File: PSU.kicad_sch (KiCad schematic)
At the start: 71 parts, among them U10 RT8293B, U14 TPS26400PWPR, U22 TLV77325PDBVR, U4 TPS7A39, U5 TPS560430XFDBVT

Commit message: last stm32h7 version
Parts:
- removed C106, C107, C108, C109, C110, C111, C53, C56: 100uF, PCM_JLCPCB:C_1206, symbol PCM_JLCPCB-Capacitors:1206,100uF
- removed C26, C33, C41, C42, C48, C49, C5, C7: 10uF, PCM_JLCPCB:C_0603, symbol PCM_JLCPCB-Capacitors:0603,10uF
- removed R119: 110k, Resistor_SMD:R_0402_1005Metric, symbol Device:R_Small
- removed R120: 8.2k, Resistor_SMD:R_0402_1005Metric, symbol Device:R_Small
- removed R130: 12k, Resistor_SMD:R_0402_1005Metric, symbol Device:R_Small
- removed R131: 20k, Resistor_SMD:R_0402_1005Metric, symbol Device:R_Small
- added C108, C109, C110, C111, C131, C156, C157, C158: 47uF, PCM_JLCPCB:C_1206, symbol PCM_JLCPCB-Capacitors:1206,47uF
- added C401: 1uF, PCM_JLCPCB:C_0402, symbol PCM_JLCPCB-Capacitors:0402,1uF
- added C402, C403, C404, C405: 10uF, PCM_JLCPCB:C_0603, symbol PCM_JLCPCB-Capacitors:0603,10uF,(2)
- added R401: 110kΩ, PCM_JLCPCB:R_0603, symbol PCM_JLCPCB-Resistors:0603,110kΩ
- added R402: 8.2kΩ, PCM_JLCPCB:R_0402, symbol PCM_JLCPCB-Resistors:0402,8.2kΩ
- added R403: 12kΩ, PCM_JLCPCB:R_0402, symbol PCM_JLCPCB-Resistors:0402,12kΩ
- added R404: 20kΩ, PCM_JLCPCB:R_0402, symbol PCM_JLCPCB-Resistors:0402,20kΩ
- added U301: STM32N657I0H3Q, User:VFBGA178_12X12_STM, symbol User:STM32N657I0H3Q
- L3: value 33u -> 22u
- U5: value TPS560430XFDBVT -> TI LMR54406DBVR
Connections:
- net +9V: now also R401.1
- net +V_OPA: now also C108.1, C109.1, C110.1, C111.1
- net -7V: now also C403.2, C405.2
- net -V_OPA: now also C131.2, C156.2, C157.2, C158.2
- net GND: now also C108.2, C109.2, C110.2, C111.2, C131.1, C156.1, C157.1, C158.1, C401.1, C402.2, C403.1, C404.2, C405.1, U301.A14 (VSS), U301.E2 (VSSAPMU), U301.E7 (VSS), U301.F1 (VSSSMPS), U301.F10 (VSS), U301.F2 (VSSSMPS), U301.F3 (VSSSMPS), U301.F4 (VSSSMPS), U301.F5 (VSSAON), U301.H10 (VSS), U301.H11 (VSS), U301.K10 (VSS), U301.K5 (VSS), U301.M4 (VSSA), U301.P1 (VSS), U301.P14 (VSS)
- net PowerPad: now also R403.2, R404.2
- net at U14.11 (ILIM): now also R404.1
- net +9VA: now reaches C129.1, D3.2, U14.15 (OUT), U14.16 (OUT)
- net +9VA: now also U4.1 (INP), U4.2 (EN), C402.1, C404.1
- net at U14.3 (UVLO): now also R401.2, R402.2
- net at U14.5 (OVP): now also R402.1, R403.1
- net at U4.3 (NR/SS): now also C401.2

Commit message: imrt1176 is added
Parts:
- removed C129: 10uF, PCM_JLCPCB:C_0603, symbol PCM_JLCPCB-Capacitors:0603,10uF,(2)
- removed C24: 4.7uF, PCM_JLCPCB:C_0805, symbol PCM_JLCPCB-Capacitors:0805,4.7uF
- removed C25, C4: 1uF, PCM_JLCPCB:C_0402, symbol PCM_JLCPCB-Capacitors:0402,1uF
- removed C27: 2.2nF, PCM_JLCPCB:C_0805, symbol PCM_JLCPCB-Capacitors:0805,2.2nF
- removed C28, C3, C6, C9: 100nF, PCM_JLCPCB:C_0402, symbol PCM_JLCPCB-Capacitors:0402,100nF,(2)
- removed C29: DNP, Capacitor_SMD:C_0805_2012Metric, symbol Device:C
- removed C30: C, Capacitor_SMD:C_0402_1005Metric, symbol Device:C
- removed C50, C65: C, symbol Device:C
- removed C57, C63, C80, C85: 10uF, PCM_JLCPCB:C_0402, symbol PCM_JLCPCB-Capacitors:0402,10uF
- removed D3: SMF20CA, PCM_JLCPCB:D_SOD-123FL, symbol PCM_JLCPCB-Diodes:TVS-Uni,SMF20CA
- removed FB3: ?, symbol Device:FerriteBead
- removed R3, R34: 47Ω, PCM_JLCPCB:R_0402, symbol PCM_JLCPCB-Resistors:0402,47Ω
- removed R31, R47: 24kΩ, PCM_JLCPCB:R_0402, symbol PCM_JLCPCB-Resistors:0402,24kΩ
- removed R32: 100kΩ, PCM_JLCPCB:R_0402, symbol PCM_JLCPCB-Resistors:0402,100kΩ
- removed R33: 22kΩ, PCM_JLCPCB:R_0402, symbol PCM_JLCPCB-Resistors:0402,22kΩ
- removed R401: 110kΩ, PCM_JLCPCB:R_0603, symbol PCM_JLCPCB-Resistors:0603,110kΩ
- removed R402: 8.2kΩ, PCM_JLCPCB:R_0402, symbol PCM_JLCPCB-Resistors:0402,8.2kΩ
- removed R403: 12kΩ, PCM_JLCPCB:R_0402, symbol PCM_JLCPCB-Resistors:0402,12kΩ
- removed R404: 20kΩ, PCM_JLCPCB:R_0402, symbol PCM_JLCPCB-Resistors:0402,20kΩ
- removed R46: 75kΩ, PCM_JLCPCB:R_0402, symbol PCM_JLCPCB-Resistors:0402,75kΩ
- removed R6: 4.3kΩ, PCM_JLCPCB:R_0603, symbol PCM_JLCPCB-Resistors:0603,4.3kΩ
- removed U10: RT8293B, Package_SO:TI_SO-PowerPAD-8, symbol User:RT8293B
- removed U14: TPS26400PWPR, User:PWP0016H-IPC_A, symbol 2025-02-23_17-32-12:TPS26400PWPR
- removed U301: STM32N657I0H3Q, User:VFBGA178_12X12_STM, symbol User:STM32N657I0H3Q
- removed U5: TI LMR54406DBVR, Package_TO_SOT_SMD:SOT-23-6, symbol User:TPS560430XF
- added C1, C19, C2, C20, C21, C22, C23, C24, C36, C37, C38, C39, C44, C48, C49, C5, C6, C7, C9: 10uF, PCM_JLCPCB:C_0402, symbol PCM_JLCPCB-Capacitors:0402,10uF
- added C11: 220nF, PCM_JLCPCB:C_0402, symbol PCM_JLCPCB-Capacitors:0402,220nF
- added C17, C18: 2.2nF, PCM_JLCPCB:C_0805, symbol PCM_JLCPCB-Capacitors:0805,2.2nF
- added C25, C26: 10u, Capacitor_SMD:C_1206_3216Metric, symbol Device:C_Small
- added C27: 100n, Capacitor_SMD:C_0603_1608Metric, symbol Device:C_Small
- added C28: 10n, Capacitor_SMD:C_0603_1608Metric, symbol Device:C_Small
- added C29: 6p8, Capacitor_SMD:C_0603_1608Metric, symbol Device:C_Small
- added C3, C4, C8: 100nF, PCM_JLCPCB:C_0402, symbol PCM_JLCPCB-Capacitors:0402,100nF
- added C30: 8p2, Capacitor_SMD:C_0603_1608Metric, symbol Device:C_Small
- added C31: 220n, Capacitor_SMD:C_0603_1608Metric, symbol Device:C_Small
- added C32, C33: 22u, Capacitor_SMD:C_0805_2012Metric, symbol Device:C_Small
- added C34: 4n7, Capacitor_SMD:C_0603_1608Metric, symbol Device:C_Small
- added C40, C42, C43, C45, C47: 2.2uF, PCM_JLCPCB:C_0402, symbol PCM_JLCPCB-Capacitors:0402,2.2uF
- added C41: 4.7uF, PCM_JLCPCB:C_0402, symbol PCM_JLCPCB-Capacitors:0402,4.7uF
- added C53, C56: 100nF, PCM_JLCPCB:C_0603, symbol PCM_JLCPCB-Capacitors:0603,100nF
- added D4, D5: B5819W, Diode_SMD:D_SOD-123, symbol Device:D_Schottky_Small
- added IC1: TPS65131RGET, symbol User:TPS65131RGET
- added J3: 9V, User:BarrelJack_GCT_DCJ200-10-A_Horizontal, symbol Connector:Jack-DC
- added L1: 4.7uH, symbol Device:L
- added L6, L7: 10u, Inductor_SMD:L_Sunlord_MWSA0518_5.4x5.2mm, symbol Device:L_Small
- added Q1: NMOS, symbol Simulation_SPICE:NMOS
- added Q2: AO3401A, Package_TO_SOT_SMD:SOT-23, symbol Transistor_FET:AO3401A
- added R11: 22kΩ, PCM_JLCPCB:R_0805, symbol PCM_JLCPCB-Resistors:0805,22kΩ
- added R17: 33kΩ, PCM_JLCPCB:R_0402, symbol PCM_JLCPCB-Resistors:0402,33kΩ
- added R18: 100kΩ, PCM_JLCPCB:R_0402, symbol PCM_JLCPCB-Resistors:0402,100kΩ
- added R2: 47Ω, PCM_JLCPCB:R_0402, symbol PCM_JLCPCB-Resistors:0402,47Ω
- added R23: 100, Resistor_SMD:R_0603_1608Metric, symbol Device:R_Small
- added R24, R27: 1M, Resistor_SMD:R_0603_1608Metric, symbol Device:R_Small
- added R25: 110k, Resistor_SMD:R_0603_1608Metric, symbol Device:R_Small
- added R26: 100k, Resistor_SMD:R_0603_1608Metric, symbol Device:R_Small
- added R28, R29: 12k, Resistor_SMD:R_0603_1608Metric, symbol Device:R_Small
- added R5: 75kΩ, PCM_JLCPCB:R_0402, symbol PCM_JLCPCB-Resistors:0402,75kΩ
- added R7: 4.7kΩ, PCM_JLCPCB:R_0402, symbol PCM_JLCPCB-Resistors:0402,4.7kΩ
- added R8: 24kΩ, PCM_JLCPCB:R_0402, symbol PCM_JLCPCB-Resistors:0402,24kΩ
- added TP1: 3.3V_Prefilter, symbol Connector:TestPoint
- added TP2: Bode, symbol Connector:TestPoint
- added TP3: FB, symbol Connector:TestPoint
- added TP4: 3.3V_GND, symbol Connector:TestPoint
- added TP5: 3.3V_Postfilter, symbol Connector:TestPoint
- added U11: RT8293B, Package_SO:SOP-8-1EP_4.57x4.57mm_P1.27mm_EP4.57x4.45mm_ThermalVias, symbol User:RT8293B
- added U13: LM74700, Package_TO_SOT_SMD:SOT-23-6, symbol Power_Management:LM74700
- added U6: MIMXRT1176CVM8A, User:BGA289C80P17X17_1400X1400X152, symbol User:MIMXRT1176CVM8A
- L3: value 22u -> 4.7uf; footprint (none) -> Inductor_SMD:L_12x12mm_H8mm
- L4: value 3.6uH -> L; footprint Inductor_SMD:L_Cenker_CKCS8040 -> (none)
- renumbered C68 to C10, C69 to C62, U22 to U8
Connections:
- net +9V is gone; now on net +9VA: D1.1
- net +3.3V: now also C51.1, L2.2, R56.1, C1.1, C2.1, C44.1, C5.1, C7.1, R17.1, TP5.1, U6.L5 (DCDC_IN_Q), U6.M5 (DCDC_IN), U6.N5 (DCDC_IN), U6.R12 (VDD_LPSR_IN), U6.U12 (VDD_SNVS_IN); no longer C35.1, L4.2
- net +9VA: now also C53.1, C56.1, J3.2, Q1.3 (S), U13.3 (EN), U13.6 (ANODE)
- net at L4.1: now also C54.1, Q1.1 (D), U13.4 (CATHODE)
- net at L3.1: now also C3.2, U11.3 (SW)
- net at L2.1: now also L3.2, C19.1, C20.1, C21.1, C22.1, R2.2, TP1.1; no longer C54.1
- net +2.5VA renamed +2.5V
- net +9-18V: no longer names the net of R12.1
- net +9-18V: now also L4.2, C23.1, C48.1, C49.1, R18.1, U11.2 (VIN); no longer L2.2
- net +V_OPA renamed +6.5V
- net -V_OPA renamed -6.5V
- net GND renamed DCDC_GND
- net DCDC_GND: now also C1.2, C11.2, C18.2, C19.2, C2.2, C20.2, C21.2, C22.2, C23.2, C24.2, C25.2, C26.2, C27.2, C28.2, C31.2, C32.2, C33.2, C34.2, C36.2, C37.2, C38.2, C39.2, C4.2, C40.2, C41.2, C42.2, C43.2, C44.2, C45.2, C47.2, C48.2, C49.2, C5.2, C53.2, C6.2, C7.2, C8.2, C9.2, IC1.19 (AGND), IC1.2 (PGND_1), IC1.25 (POWERPAD), IC1.3 (PGND_2), J3.1, L7.2, R11.2, R25.1, R28.1, R29.1, R7.2, R8.2, TP4.1, U11.4 (GND), U11.9 (GND), U6.A1 (VSS1), U6.A17 (VSS1), U6.B7 (VSS1), U6.C10 (VSS1), U6.C12 (VSS1), U6.C14 (VSS1), U6.C8 (VSS1), U6.D4 (VSS1), U6.F11 (VSS1), U6.F12 (VSS1), U6.F13 (VSS1), U6.G10 (VSS2), U6.G11 (VSS2), U6.G15 (VSS2), U6.G3 (VSS1), U6.G7 (VSS1), U6.G8 (VSS1), U6.G9 (VSS1), U6.H11 (VSS2), U6.H7 (VSS2), U6.J11 (VSS2), U6.J7 (VSS2), U6.K11 (VSS2), U6.K6 (DCDC_GND), U6.K7 (DCDC_GND), U6.L10 (VSS2), U6.L11 (VSS2), U6.L15 (VSS2), U6.L3 (VSS2), U6.L6 (DCDC_GND), U6.P14 (VSS2), U6.P4 (VSS2), U6.R4 (VSS2), U6.R7 (VSS3), U6.T11 (TEST_MODE), U6.T12 (VSS3), U6.U1 (VSS3), U6.U17 (VSS3); no longer L3.2
- new net: IC1.7 (BSW), Q2.1 (G)
- new net: C26.1, L6.1, Q2.3 (D)
- new net: C29.2, IC1.22 (FBP), R24.1, R25.2
- new net: C27.1, IC1.10 (ENN), IC1.11 (PSN), IC1.4 (VIN), IC1.8 (ENP), IC1.9 (PSP), R23.1
- new net: C17.2, R11.1
- new net: C3.1, U11.1 (BOOT)
- new net: R5.2, R8.1, TP3.1, U11.5 (FB)
- new net: C17.1, C18.1, U11.6 (COMP)
- new net: R18.2, U11.7 (EN)
- new net: C4.1, U11.8 (SS/PG)
- new net: L1.1, U6.T3 (DCDC_LP), U6.U3 (DCDC_LP)
- new net: L1.2, U6.T4 (DCDC_LN), U6.U4 (DCDC_LN)
- new net: D5.1 (K), IC1.13 (OUTN_1), IC1.14 (OUTN_2), L7.1
- new net: C11.1, R17.2, U6.P3 (DCDC_PSWITCH)
- new net: C30.1, IC1.16 (FBN), R26.1, R27.2
- new net: D4.2 (A), IC1.1 (INP_1), IC1.24 (INP_2), L6.2
- new net: C31.1, IC1.17 (VREF), R26.2
- new net: C34.1, IC1.18 (CN)
- new net: C28.1, IC1.21 (CP)
- new net: U6.F6 (NVCC_EMC1), U6.F7 (NVCC_EMC1), U6.G6 (NVCC_EMC1)
- new net: U6.H6 (NVCC_EMC2), U6.J6 (NVCC_EMC2)
- new net: C56.2, U13.1 (VCAP)
- new net: Q1.2 (G), U13.5 (GATE)
- new net: R2.1, R5.1, TP2.1
- new net +12V: C29.1, C33.1, D4.1 (K), IC1.23 (VPOS), R24.2, R29.2
- new net +5V: C25.1, IC1.5 (INN_1), IC1.6 (INN_2), Q2.2 (S), R23.2
- new net -12V: C30.2, C32.1, D5.2 (A), IC1.15 (VNEG), R27.1, R28.2
- new net 1.15V_DCDC: C24.1, C35.1, C36.1, C37.1, C38.1, C39.1, U6.K8 (DCDC_DIG), U6.K9 (DCDC_DIG), U6.L7 (DCDC_DIG_SENSE), U6.L8 (DCDC_DIG)
- new net 1.8V_DCDC: C6.1, C9.1, U6.F9 (VDD_MIPI_1P8), U6.M6 (DCDC_ANA_SENSE), U6.M7 (DCDC_ANA), U6.M8 (DCDC_ANA)
- new net DCDC_MODE: C8.1, R7.1, U6.N4 (DCDC_MODE)
- new net VDDA_1P0: C42.1, C43.1, U6.F10 (VDD_MIPI_1P0), U6.N11 (VDDA_1P0)
- new net VDD_LPSR_ANA: C40.1, U6.P12 (VDD_LPSR_ANA)
- new net VDD_LPSR_DIG: C41.1, U6.P11 (VDD_LPSR_DIG)
- new net VDD_SNVS_ANA: C45.1, C47.1, U6.U11 (NVCC_SNVS), U6.U14 (VDD_SNVS_ANA)
- new net VDD_SOC_IN: U6.H10 (VDD_SOC_IN), U6.H8 (VDD_SOC_IN), U6.H9 (VDD_SOC_IN), U6.J10 (VDD_SOC_IN), U6.J8 (VDD_SOC_IN), U6.J9 (VDD_SOC_IN), U6.K10 (VDD_SOC_IN)
- no-connect marks 6 -> 2
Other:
- note added: "+V_OPA 6.5V 50mA -V_OPA -6.5V 50mA +3.3V 3.3V 500mA +1.8V 1.8V 1.2A"
- note added: "5V to +12V / -12V Regulator"
- note added: "9V 50+200+330+100"
- note added: "VCC(max) = 12V - Limited by Vgs (Q1)!"
- note added: "https://www.we-online.com/components/products/datasheet/7447713047.pdf"
- note removed: "-kisebb MOSFET U21-re -TP2121 ellenállásait kiszámolni -dc-dc be- és kimenő szűrő kiszámolni -tps7a39 ellenállásait kiszámolni +-5V-os konverternek kimenő szűrőt tervezni"
- note removed: "OMRON G6K-2F-Y-TR DC5"
- note removed: "https://www.ti.com/lit/an/slvae10/slvae10.pdf?utm_source=chatgpt.com&ts=1755168580112&ref_url=https%253A%252F%252Fchatgpt.com%252F"
- moved on the sheet: C10, C51, C52, C54, C55, C62, D1, L2, R12, R56, U8

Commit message: added renesas RA8P1
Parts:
- removed C1, C2, C23, C24, C35, C36, C37, C38, C39, C44, C48, C49, C5, C6, C7, C9: 10uF, PCM_JLCPCB:C_0402, symbol PCM_JLCPCB-Capacitors:0402,10uF
- removed C11: 220nF, PCM_JLCPCB:C_0402, symbol PCM_JLCPCB-Capacitors:0402,220nF
- removed C40, C42, C43, C45, C47: 2.2uF, PCM_JLCPCB:C_0402, symbol PCM_JLCPCB-Capacitors:0402,2.2uF
- removed C53, C56: 100nF, PCM_JLCPCB:C_0603, symbol PCM_JLCPCB-Capacitors:0603,100nF
- removed C8: 100nF, PCM_JLCPCB:C_0402, symbol PCM_JLCPCB-Capacitors:0402,100nF
- removed Q1: NMOS, symbol Simulation_SPICE:NMOS
- removed R17: 33kΩ, PCM_JLCPCB:R_0402, symbol PCM_JLCPCB-Resistors:0402,33kΩ
- removed R7: 4.7kΩ, PCM_JLCPCB:R_0402, symbol PCM_JLCPCB-Resistors:0402,4.7kΩ
- removed U13: LM74700, Package_TO_SOT_SMD:SOT-23-6, symbol Power_Management:LM74700
- removed U6: MIMXRT1176CVM8A, User:BGA289C80P17X17_1400X1400X152, symbol User:MIMXRT1176CVM8A
- added C1, C11, C2, C24, C35, C36, C37, C38, C39, C40, C42, C43, C44, C45, C47, C5, C6, C60, C64, C65, C68, C69, C7, C70, C71, C72, C73, C74, C75, C8, C9: 4.7uF, PCM_JLCPCB:C_0402, symbol PCM_JLCPCB-Capacitors:0402,4.7uF
- added C23, C48, C49, C81: 10uF, PCM_JLCPCB:C_0805, symbol PCM_JLCPCB-Capacitors:0805,10uF,(2)
- added D6: SS14, PCM_JLCPCB:D_SMA, symbol PCM_JLCPCB-Diodes:Schottky,SS14
- added F1: 1A, Fuse:Fuse_0805_2012Metric, symbol Device:Fuse
- added IC2: R7KA8P1KFLCAB#UC0, User:BGA-225_15x15_11.0x11.0mm, symbol User:R7KA8P1KFLCAB#UC0
- C41: Stock 4921316 -> 4366811
- L1: footprint (none) -> Inductor_SMD:L_Wuerth_MAPI-4030
- L4: value L -> 1uH; footprint (none) -> Inductor_SMD:L_1008_2520Metric
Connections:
- net VDD_LPSR_DIG is gone; now on net +3.3V: C41.1
- net +3.3V: now also C1.1, C11.1, C2.1, C24.1, C35.1, C36.1, C37.1, C38.1, C39.1, C40.1, C42.1, C43.1, C44.1, C45.1, C5.1, C6.1, C7.1, C70.1, C8.1, C9.1, IC2.A10 (VCC_DCDC_2), IC2.A9 (VCC_DCDC_1), IC2.B10 (VCC_DCDC_4), IC2.B9 (VCC_DCDC_3), IC2.E10 (VCC_07), IC2.E5 (VCC_08), IC2.F14 (VCC_05), IC2.F5 (VCC_09), IC2.G12 (VCC_03), IC2.G13 (VCC_USBHS), IC2.G5 (VCC_10), IC2.J12 (VCC_02), IC2.J13 (AVCC_USBHS), IC2.J6 (VCC2_15), IC2.K13 (VCC_01), IC2.K5 (VCC2_14), IC2.L14 (VBATT), IC2.N1 (VCC2_12), IC2.R15 (VCC_USB)
- net at L4.2, R12.1, R18.1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: now also C23.1, C48.1, C49.1, C81.1
- net at L1.1: now also C47.1, C60.1, C64.1, C65.1, C68.1, C69.1, C71.1, C72.1, C73.1, C74.1, C75.1, IC2.E8 (VCL5), IC2.F8 (VCL6), IC2.F9 (VCL4), IC2.G8 (VCL7), IC2.G9 (VCL3), IC2.H8 (VCL8), IC2.H9 (VCL2), IC2.J8 (VCL9), IC2.J9 (VCL1), IC2.K8 (VCL10), IC2.K9 (VCL0), IC2.L9 (VCL11)
- net at L1.2: now also IC2.A6 (VLO_1), IC2.A7 (VLO_2), IC2.B6 (VLO_3), IC2.B7 (VLO_4)
- net +9VA renamed +7V
- net +7V: no longer D1.1, J3.2
- net DCDC_GND renamed GND
- net GND: now also C1.2, C11.2, C2.2, C23.2, C24.2, C35.2, C36.2, C37.2, C38.2, C39.2, C40.2, C42.2, C43.2, C44.2, C45.2, C47.2, C48.2, C49.2, C5.2, C6.2, C60.2, C64.2, C65.2, C68.2, C69.2, C7.2, C70.2, C71.2, C72.2, C73.2, C74.2, C75.2, C8.2, C81.2, C9.2, IC2.A8 (VSS_DCDC_1), IC2.B8 (VSS_DCDC_2), IC2.E6 (VSS_08), IC2.E7 (VSS5), IC2.E9 (VSS_07), IC2.F10 (VSS4), IC2.F13 (VSS_03), IC2.F15 (VSS_05), IC2.F6 (VSS_09), IC2.F7 (VSS6), IC2.G10 (VSS3), IC2.G6 (VSS_10), IC2.G7 (VSS7), IC2.H10 (VSS2), IC2.H12 (VSS_02), IC2.H14 (VSS2_USBHS), IC2.H15 (VSS1_USBHS), IC2.H6 (VSS_15), IC2.H7 (VSS8), IC2.J10 (VSS1), IC2.J7 (VSS9), IC2.K10 (VSS0), IC2.K6 (VSS_14), IC2.K7 (VSS10), IC2.L15 (VSS_01), IC2.L8 (VSS11), IC2.N3 (VSS_MIPI), IC2.N9 (AVSS0), IC2.P15 (VSS_USB), IC2.P8 (VREFL), IC2.P9 (VREFL0), IC2.R4 (VSS_12)
- new net: D1.1, D6.2, J3.2
- new net: D6.1, F1.1
- no-connect marks 2 -> 3
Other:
- note added: "TPS2596"
- moved on the sheet: C10, C62, D1, L1, U8

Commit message: progressed with SDRAM layout
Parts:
- removed C10: 10uF, PCM_JLCPCB:C_0402, symbol PCM_JLCPCB-Capacitors:0402,10uF
- removed C25, C26: 10u, Capacitor_SMD:C_1206_3216Metric, symbol Device:C_Small
- removed C27: 100n, Capacitor_SMD:C_0603_1608Metric, symbol Device:C_Small
- removed C28: 10n, Capacitor_SMD:C_0603_1608Metric, symbol Device:C_Small
- removed C29: 6p8, Capacitor_SMD:C_0603_1608Metric, symbol Device:C_Small
- removed C3: 100nF, PCM_JLCPCB:C_0402, symbol PCM_JLCPCB-Capacitors:0402,100nF
- removed C30: 8p2, Capacitor_SMD:C_0603_1608Metric, symbol Device:C_Small
- removed C31: 220n, Capacitor_SMD:C_0603_1608Metric, symbol Device:C_Small
- removed C32, C33: 22u, Capacitor_SMD:C_0805_2012Metric, symbol Device:C_Small
- removed C34: 4n7, Capacitor_SMD:C_0603_1608Metric, symbol Device:C_Small
- removed C402, C403: 10uF, PCM_JLCPCB:C_0603, symbol PCM_JLCPCB-Capacitors:0603,10uF,(2)
- removed C51, C54: C, symbol Device:C
- removed C55: ?, symbol Device:C_Polarized
- removed D4, D5: B5819W, Diode_SMD:D_SOD-123, symbol Device:D_Schottky_Small
- removed F1: 1A, Fuse:Fuse_0805_2012Metric, symbol Device:Fuse
- removed L2: L, symbol Device:L
- removed Q2: AO3401A, Package_TO_SOT_SMD:SOT-23, symbol Transistor_FET:AO3401A
- removed R12: 0Ω, PCM_JLCPCB:R_0402, symbol PCM_JLCPCB-Resistors:0402,0Ω
- removed R23: 100, Resistor_SMD:R_0603_1608Metric, symbol Device:R_Small
- removed R24, R27: 1M, Resistor_SMD:R_0603_1608Metric, symbol Device:R_Small
- removed R25: 110k, Resistor_SMD:R_0603_1608Metric, symbol Device:R_Small
- removed R26: 100k, Resistor_SMD:R_0603_1608Metric, symbol Device:R_Small
- removed R28, R29: 12k, Resistor_SMD:R_0603_1608Metric, symbol Device:R_Small
- removed R56: 0, symbol Device:R_Small
- added C10, C30: 4.7uF, PCM_JLCPCB:C_0402, symbol PCM_JLCPCB-Capacitors:0402,4.7uF
- added C106, C107: 6.8pF, PCM_JLCPCB:C_0402, symbol PCM_JLCPCB-Capacitors:0402,6.8pF
- added C25, C26, C28, C29: 10uF, PCM_JLCPCB:C_0402, symbol PCM_JLCPCB-Capacitors:0402,10uF
- added C27, C3, C54, C84, C85, C86: 100nF, PCM_JLCPCB:C_0402, symbol PCM_JLCPCB-Capacitors:0402,100nF,(2)
- added C31: 220nF, PCM_JLCPCB:C_0402, symbol PCM_JLCPCB-Capacitors:0402,220nF
- added C32, C33, C34, C51, C55, C94, C95, C96: 47uF, PCM_JLCPCB:C_1206, symbol PCM_JLCPCB-Capacitors:1206,47uF
- added C53: 1uF, PCM_JLCPCB:C_0603, symbol PCM_JLCPCB-Capacitors:0603,1uF
- added C82, C83: 10uF, PCM_JLCPCB:C_0805, symbol PCM_JLCPCB-Capacitors:0805,10uF,(2)
- added C97: 10nF, Capacitor_SMD:C_0603_1608Metric, symbol Device:C
- added C98: 4.7nF, Capacitor_SMD:C_0603_1608Metric, symbol Device:C
- added D4, D7: B5819W, PCM_JLCPCB:D_SOD-123, symbol PCM_JLCPCB-Diodes:Schottky,B5819W
- added Q1: AO3401A, PCM_JLCPCB:Q_SOT-23, symbol PCM_JLCPCB-Transistors:PMOS,AO3401A
- added R12: 1, PCM_JLCPCB:R_0402, symbol Device:R
- added R23, R25: 47Ω, PCM_JLCPCB:R_0402, symbol PCM_JLCPCB-Resistors:0402,47Ω
- added R24: 100Ω, PCM_JLCPCB:R_0603, symbol PCM_JLCPCB-Resistors:0603,100Ω
- added R26, R28: 100kΩ, PCM_JLCPCB:R_0402, symbol PCM_JLCPCB-Resistors:0402,100kΩ
- added R27, R48: 510kΩ, PCM_JLCPCB:R_0402, symbol PCM_JLCPCB-Resistors:0402,510kΩ
- added R44: 12kΩ, PCM_JLCPCB:R_0402, symbol PCM_JLCPCB-Resistors:0402,12kΩ
- added R45: 110kΩ, PCM_JLCPCB:R_0603, symbol PCM_JLCPCB-Resistors:0603,110kΩ
- added R46: 8.2kΩ, PCM_JLCPCB:R_0603, symbol PCM_JLCPCB-Resistors:0603,8.2kΩ
- added R47: 1.5kΩ, PCM_JLCPCB:R_0402, symbol PCM_JLCPCB-Resistors:0402,1.5kΩ
- added TP10: FB3, Thunderscope_Rev5.1:GEN_TP_PCB, symbol Connector:TestPoint
- added TP6: Bode3, Thunderscope_Rev5.1:GEN_TP_PCB, symbol Connector:TestPoint
- added TP7: 7V, Thunderscope_Rev5.1:GEN_TP_PCB, symbol Connector:TestPoint
- added TP8: -7V, Thunderscope_Rev5.1:GEN_TP_PCB, symbol Connector:TestPoint
- added TP9: FB2, Thunderscope_Rev5.1:GEN_TP_PCB, symbol Connector:TestPoint
- added U13: TPS259630, Package_SO:TI_SO-PowerPAD-8, symbol User:TPS259630
- C52: value ? -> 100u, 60mR; footprint (none) -> Capacitor_Tantalum_SMD:CP_EIA-7343-31_Kemet-D
- L3: footprint Inductor_SMD:L_12x12mm_H8mm -> User:WE-PD_1030P
- L4: value 1uH -> 22uH; footprint Inductor_SMD:L_1008_2520Metric -> Inductor_SMD:L_7.3x7.3_H3.5
- L6, L7: footprint Inductor_SMD:L_Sunlord_MWSA0518_5.4x5.2mm -> Inductor_SMD:L_Sunlord_MWSA0518S
- TP1: value 3.3V_Prefilter -> 3.3V; footprint (none) -> Thunderscope_Rev5.1:GEN_TP_PCB
- TP2, TP3: footprint (none) -> Thunderscope_Rev5.1:GEN_TP_PCB
- TP4: footprint (none) -> TestPoint:TestPoint_Pad_1.0x1.0mm
- TP5: value 3.3V_Postfilter -> Bode2; footprint (none) -> Thunderscope_Rev5.1:GEN_TP_PCB
- U17: renamed from IC1; footprint (none) -> Package_DFN_QFN:VQFN-24-1EP_4x4mm_P0.5mm_EP2.5x2.5mm_ThermalVias
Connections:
- net +12V is gone; now on net +7V: U17.23 (VPOS)
- net +5V is gone; now on net +3.3V: U17.5 (IN_N), U17.6 (IN_N_2)
- net -12V is gone; now on net -7V: U17.15 (VNEG)
- net +2.5V: now also IC2.N8 (AVCC0), IC2.R8 (VREFH), IC2.R9 (VREFH0)
- net +3.3V: now also C19.1, C20.1, C21.1, C22.1, IC2.P4 (AVCC_MIPI), L3.2, R2.2, TP1.1, C10.1, C30.1, Q1.2 (S); no longer TP5.1
- net +7V: now also C55.1, C94.1, C95.1, C96.1, D7.1, R23.2, TP7.1
- net -7V: now also C32.2, C33.2, C34.2, C51.2, D4.2, R25.1, TP8.1
- net GND: now also U17.11 (PSN), U17.9 (PSP), C10.2, C25.2, C26.2, C27.2, C28.2, C29.2, C30.2, C31.1, C32.1, C33.1, C34.1, C51.1, C53.2, C54.2, C55.2, C82.2, C83.2, C84.2, C85.2, C86.2, C94.2, C95.2, C96.2, C97.2, C98.2, R26.2, R46.2, R47.2, U13.1 (GND), U13.9 (EPAD)
- net at U17.7 (BSW): now also Q1.1 (G)
- net at L6.1: now also C26.1, C28.1, C29.1, Q1.3 (D)
- net at U17.22 (FBP): now also C106.2, R26.1, R48.1, TP9.1
- net MCU_DCDC_OUT: now reaches C47.1, C60.1, C64.1, C65.1, C68.1, C69.1, C71.1, C72.1, C73.1, C74.1, C75.1, IC2.E8 (VCL5), IC2.F8 (VCL6), IC2.F9 (VCL4), IC2.G8 (VCL7), IC2.G9 (VCL3), IC2.H8 (VCL8), IC2.H9 (VCL2), IC2.J8 (VCL9), IC2.J9 (VCL1), IC2.K8 (VCL10), IC2.K9 (VCL0), IC2.L9 (VCL11), L1.1
- net at C23.1, C48.1, C49.1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: now also C82.1, C83.1, R12.1
- net at C52.1: now also R12.2
- net at U17.10 (ENN), U17.4 (VIN), U17.8 (ENP): now also C27.1, R24.2; no longer U17.11 (PSN), U17.9 (PSP)
- net at U11.1 (BOOT): now also C3.1
- net at L3.1, U11.3 (SW): now also C3.2
- net at L7.1, U17.13 (OUT_N), U17.14 (OUT_N_2): now also D4.1
- net at U17.16 (FBN): now also C107.1, R27.2, R28.2, TP10.1
- net at L4.1: now also U13.5 (OUT)
- net at L6.2, U17.1 (INP), U17.24 (INP_2): now also D7.2
- net at U17.12 (NC): now also U17.20 (NC_2)
- net at U17.17 (VREF): now also C31.2, R28.1
- net at U17.18 (CN): now also C98.1
- net at U17.21 (CP): now also C97.1
- net at D6.1: now also C54.1, C84.1, C85.1, C86.1, R45.1, U13.4 (IN)
- new net: C106.1, R23.1, R48.2, TP5.1
- new net: C25.1, R24.1
- new net: R44.1, R45.2, U13.3 (UVLO)
- new net: R44.2, R46.1, U13.8 (OVLO)
- new net: C107.2, R25.2, R27.1, TP6.1
- new net: C53.1, U13.2 (dVdt)
- new net: R47.1, U13.7 (ILIMIT)
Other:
- note added: "+3.3V to bipolar 7V converter"
- note added: "Ceff=56uF"
- note added: "Ctarget=10uF C@19V=10.38uF C@8=26.76uF"
- note added: "UVLO=7.73V OVLO=19.05V"
- note removed: "5V to +12V / -12V Regulator"
- note removed: "TPS2596"
- note removed: "VCC(max) = 12V - Limited by Vgs (Q1)!"
- note removed: "https://www.we-online.com/components/products/datasheet/7447713047.pdf"
- moved on the sheet: C1, C108, C109, C11, C110, C111, C131, C156, C157, C158, C17, C18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

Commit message: layout progress
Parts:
- removed C62: 10uF, PCM_JLCPCB:C_0402, symbol PCM_JLCPCB-Capacitors:0402,10uF
- removed U8: TLV77325PDBVR, Package_TO_SOT_SMD:SOT-23-5, symbol Regulator_Linear:AP2127K-3.3
- added C62: 4.7uF, PCM_JLCPCB:C_0402, symbol PCM_JLCPCB-Capacitors:0402,4.7uF
- added C89: 10uF, PCM_JLCPCB:C_0402, symbol PCM_JLCPCB-Capacitors:0402,10uF
- added TP11: +6.5V, TestPoint:TestPoint_Pad_1.0x1.0mm, symbol Connector:TestPoint
- added TP12: -6.5V, TestPoint:TestPoint_Pad_1.0x1.0mm, symbol Connector:TestPoint
- U17: footprint Package_DFN_QFN:VQFN-24-1EP_4x4mm_P0.5mm_EP2.5x2.5mm_ThermalVias -> User:VQFN-24-1EP_4x4mm_P0.5mm_EP2.5x2.5mm_ThermalVias
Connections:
- net +2.5V is gone; now on net +3.3V: IC2.N8 (AVCC0), IC2.R8 (VREFH), IC2.R9 (VREFH0)
- net +3.3V: now also C25.1, R24.1, C62.1
- net +6.5V: now also TP11.1
- net -6.5V: now also TP12.1
- net GND: now also C62.2, C89.2
- net at U17.12 (NC): no longer U17.20 (NC_2)
- net at C26.1, C28.1, C29.1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: now also C89.1
- no-connect marks 3 -> 4
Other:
- note added: "+-7V to +-6.5V LDO"
- note added: "MCU Power"
- note added: "Nominal 9V to 18V input to 3.3V bus converter"
- note removed: "+V_OPA 6.5V 50mA -V_OPA -6.5V 50mA +3.3V 3.3V 500mA +1.8V 1.8V 1.2A"
- note removed: "9V 50+200+330+100"
- company: (none) -> KVAD
- title: (none) -> Project Y
- moved on the sheet: C10

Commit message: progressed with the layout
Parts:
- added C12, C13, C46: 10uF, PCM_JLCPCB:C_0402, symbol PCM_JLCPCB-Capacitors:0402,10uF
- added C58, C61, C90, C91: 4.7uF, PCM_JLCPCB:C_0402, symbol PCM_JLCPCB-Capacitors:0402,4.7uF
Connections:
- net +3.3V: now also C12.1, C13.1, C46.1
- net GND: now also C12.2, C13.2, C46.2, C58.2, C61.2, C90.2, C91.2
- net MCU_DCDC_OUT: now also C58.1, C61.1, C90.1, C91.1
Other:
- moved on the sheet: C106, C107, C25, C26, C27, C28, C29, C31, C32, C33, C34, C51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

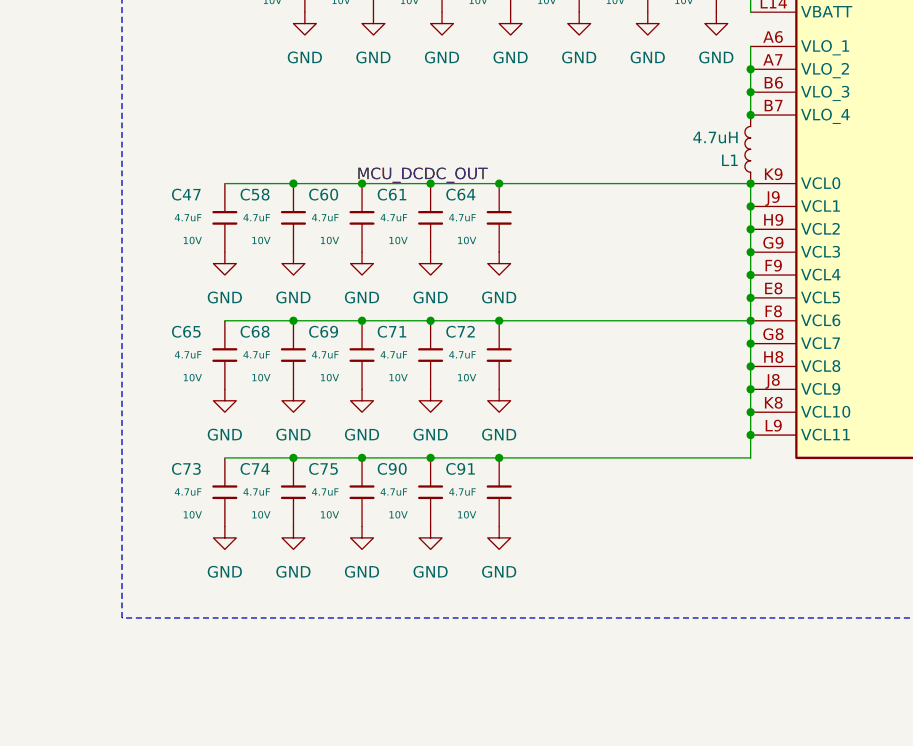
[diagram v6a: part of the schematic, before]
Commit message: DCDC upgraded
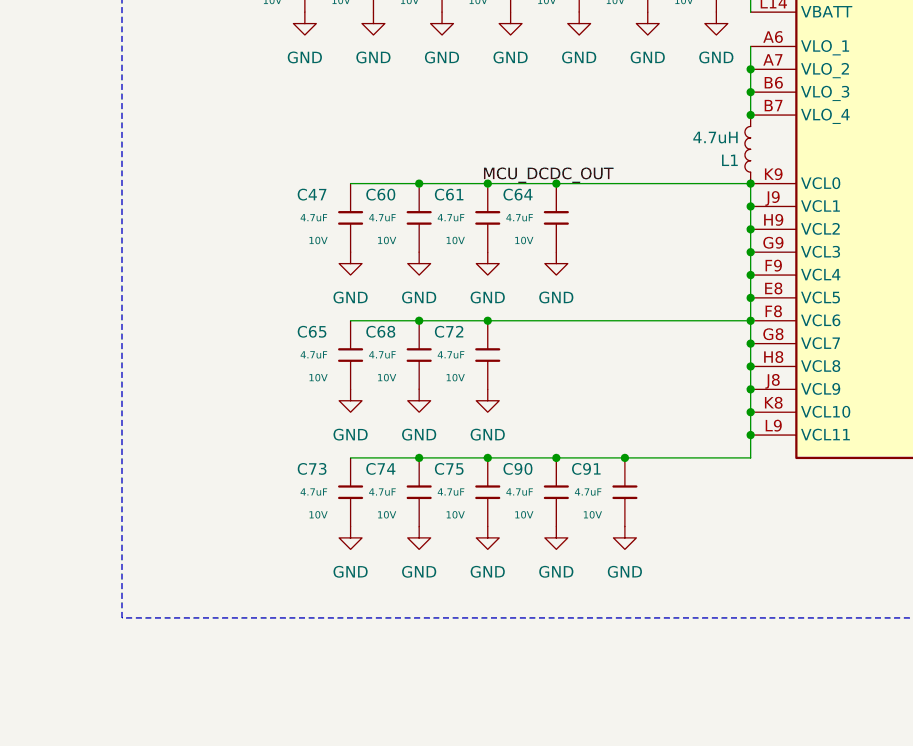
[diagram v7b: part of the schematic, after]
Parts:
- removed C58, C69, C71: 4.7uF, PCM_JLCPCB:C_0402, symbol PCM_JLCPCB-Capacitors:0402,4.7uF
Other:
- moved on the sheet: C47, C60, C61, C64, C65, C68, C72, C73, C74, C75, C90, C91

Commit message: layout is almost finished
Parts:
- removed C1, C2, C30, C38, C44, C8, C9: 4.7uF, PCM_JLCPCB:C_0402, symbol PCM_JLCPCB-Capacitors:0402,4.7uF
- removed C12, C13, C25, C46: 10uF, PCM_JLCPCB:C_0402, symbol PCM_JLCPCB-Capacitors:0402,10uF
- removed C27: 100nF, PCM_JLCPCB:C_0402, symbol PCM_JLCPCB-Capacitors:0402,100nF,(2)
- removed Q1: AO3401A, PCM_JLCPCB:Q_SOT-23, symbol PCM_JLCPCB-Transistors:PMOS,AO3401A
- removed R24: 100Ω, PCM_JLCPCB:R_0603, symbol PCM_JLCPCB-Resistors:0603,100Ω
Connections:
- net +3.3V: now also C26.1, C28.1, C29.1, C89.1, L6.1, U17.10 (ENN), U17.4 (VIN), U17.8 (ENP)
- no-connect marks 4 -> 5
